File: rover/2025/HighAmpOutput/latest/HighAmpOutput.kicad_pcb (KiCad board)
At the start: 4 copper layers, 90.9 x 51 mm, 22 parts, among them J1 JST2_Pin, U1 EC5_Connector, U10 XT60PM-F, U11 XT60PM-F, U12 XT60PM-F, U2 HSS-VN7004SLHTR, U3 XT60-F, U4 XT60-F, U5 XT60-F, U6 XT60-F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

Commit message: .
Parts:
- removed U10, U11, U9: XT60PM-F, RoverFootprint:AMASS_XT60PW-F_1x02_P7.20mm_Horizontal
- added D2: R, LED_SMD:LED_0805_2012Metric_Pad1.15x1.40mm_HandSolder, F.Cu at (147.7, 83.0)
- added R2: 15k, Resistor_SMD:R_0805_2012Metric_Pad1.20x1.40mm_HandSolder, F.Cu at (147.7, 86.0)
- added R5: 1K, Resistor_SMD:R_0805_2012Metric_Pad1.20x1.40mm_HandSolder, F.Cu at (147.7, 88.9)
- added U13: XT60-F, RoverFootprint:AMASS_XT60-F_1x02_P7.20mm_Vertical, F.Cu at (164.7, 90.1)
- added U14: XT60-F, RoverFootprint:AMASS_XT60-F_1x02_P7.20mm_Vertical, F.Cu at (164.7, 100.4)
- D1: value LED -> R
- moved U4 126.8 mm to (164.7, 38.9), turned to 0 degrees
- moved U3 121.3 mm to (164.7, 28.6), turned to 0 degrees
- moved U6 108.9 mm to (164.7, 59.4), turned to 0 degrees
- moved U12 106.8 mm to (207.0, 39.9)
- moved U5 105.8 mm to (164.7, 49.1), turned to 0 degrees
- moved U1 99.3 mm to (31.8, 139.2), turned to 0 degrees
- moved J1 98.0 mm to (63.5, 153.0), turned to 0 degrees
- moved U7 94.3 mm to (164.7, 69.6), turned to 0 degrees
- moved U8 93.9 mm to (164.7, 79.9), turned to 0 degrees
- moved U2 72.1 mm to (63.3, 145.5)
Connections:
- net /Board/+24v renamed +24V
- net /Board/Vinput renamed +24V_I
- R1 pad 1: GND -> Net-(U2-FR_DIAG)
- R1 pad 2: Net-(U2-FR_DIAG) -> GND
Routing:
- net Net-(U2-INPUT): track 0.00 -> 10.9 mm
- net GND: vias 0 -> 54
- net +24V: vias 8 -> 0
- added copper zone on In1.Cu, net +24V_I
- added copper zone on B.Cu, net GND
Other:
- board size 90.9 x 51 mm -> 90.9 x 113.4 mm

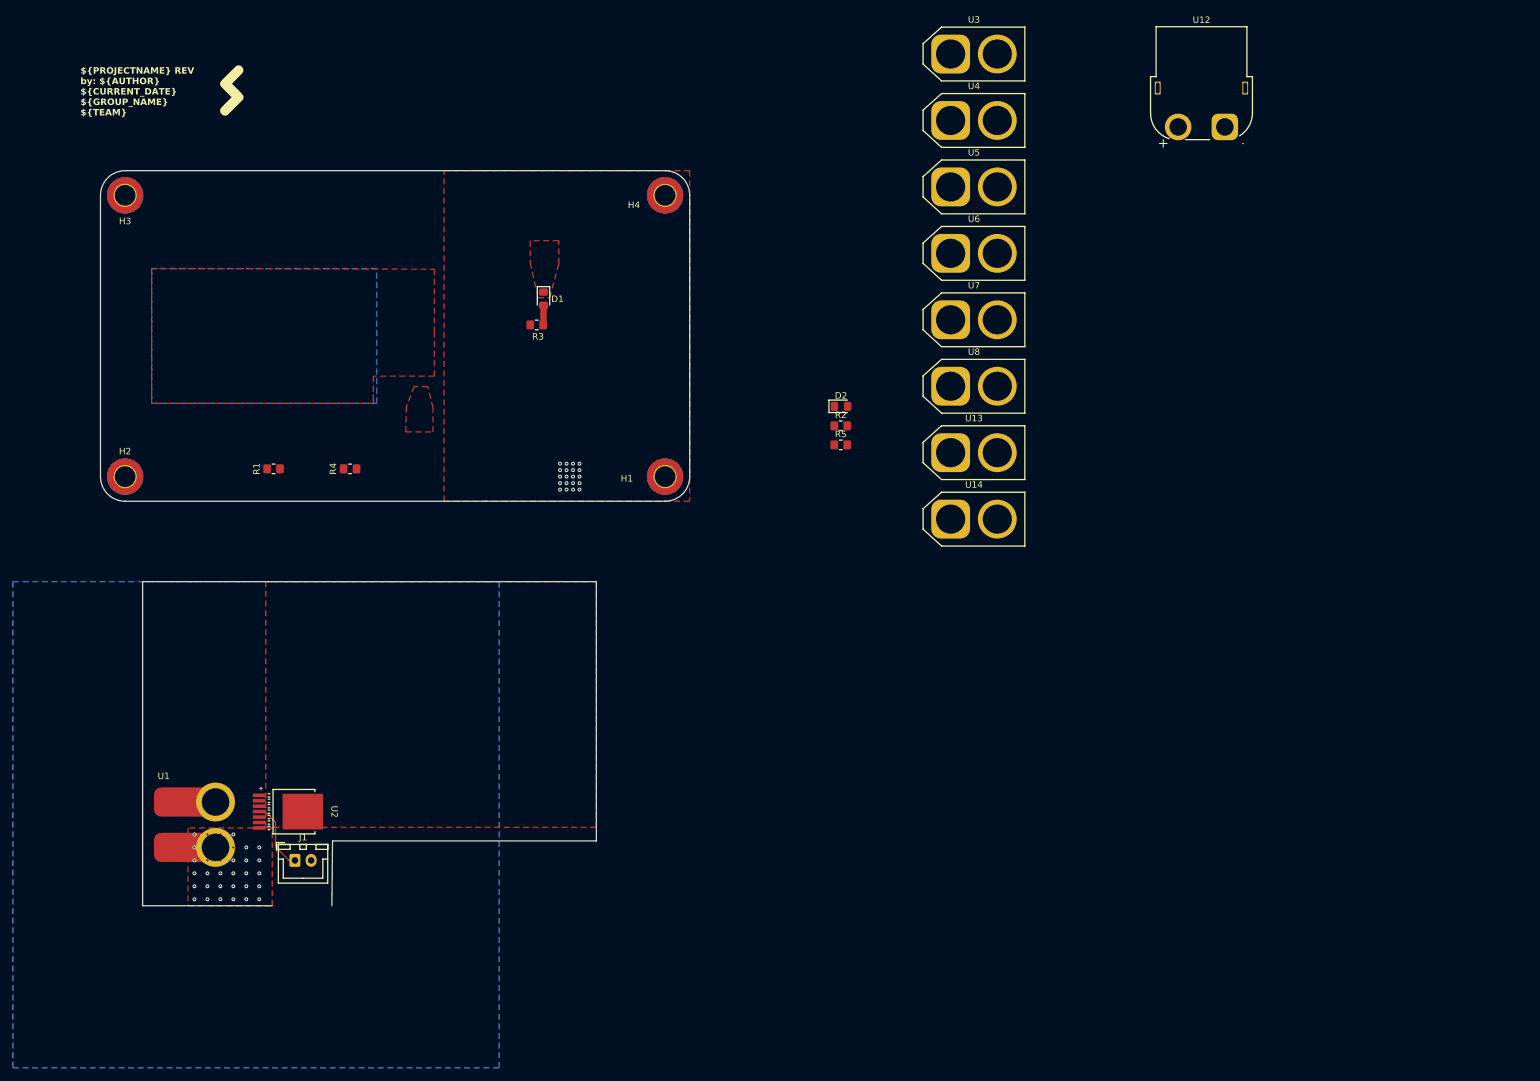
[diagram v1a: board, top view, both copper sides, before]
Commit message: Avancement PCB HighAmpOutput
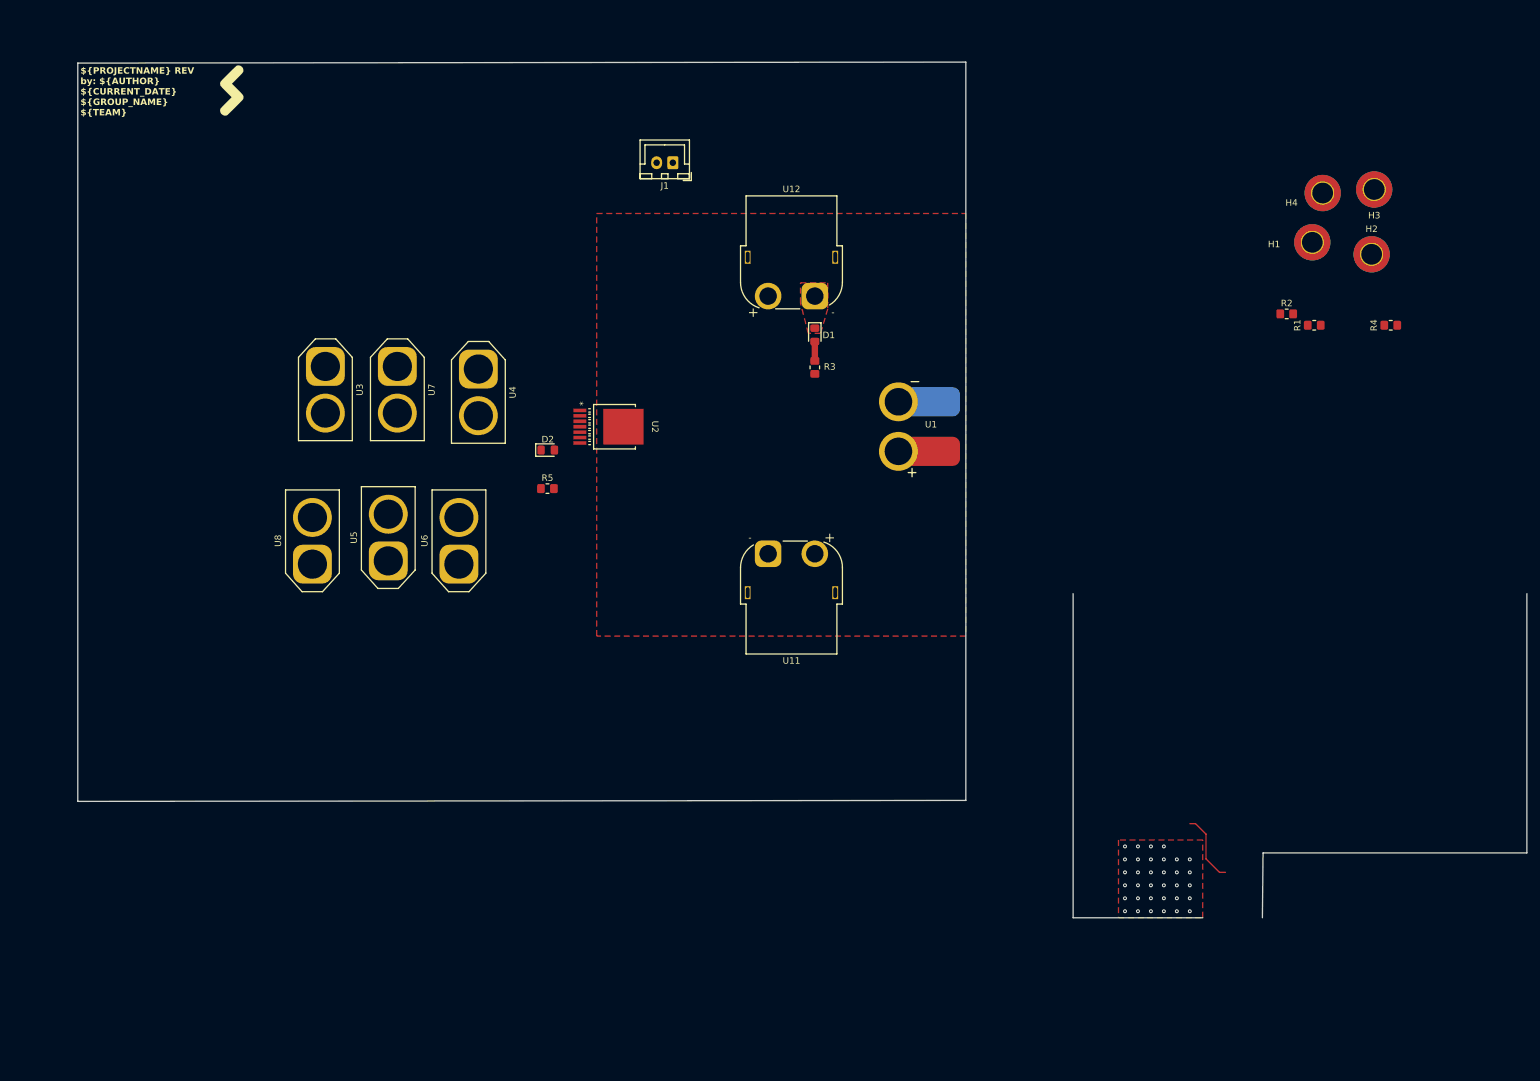
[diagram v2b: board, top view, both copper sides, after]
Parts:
- removed U13, U14: XT60-F, RoverFootprint:AMASS_XT60-F_1x02_P7.20mm_Vertical
- added U11: XT60PM-F, RoverFootprint:AMASS_XT60PW-F_1x02_P7.20mm_Horizontal, F.Cu at (136.5, 105.7)
- moved H2 195.3 mm to (229.6, 59.5)
- moved H3 192.7 mm to (230.0, 49.5)
- moved R1 162.1 mm to (220.8, 70.5)
- moved R4 162.1 mm to (232.6, 70.5)
- moved U1 141.8 mm to (166.1, 93.9), turned to 180 degrees
- moved J1 122.4 mm to (121.8, 45.4), turned to 180 degrees
- moved U3 107.8 mm to (68.2, 76.8), turned to -90 degrees
- moved H1 106.2 mm to (220.4, 57.6)
- moved U5 104.2 mm to (77.9, 106.8), turned to 90 degrees
- moved U8 102.2 mm to (66.2, 107.3), turned to 90 degrees
- moved H4 101.5 mm to (222.1, 50.0)
- moved U6 89.7 mm to (88.8, 107.3), turned to 90 degrees
- moved U7 85.7 mm to (79.3, 76.8), turned to -90 degrees
- moved U4 82.3 mm to (91.8, 77.2), turned to -90 degrees
- moved U2 77.3 mm to (112.8, 86.1)
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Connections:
- U12 pad : (no net) -> +24V_I
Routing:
- net GND: vias 54 -> 34
- removed copper zone on B.Cu, net +24V
- removed copper zone on F.Cu, net +24V
- removed copper zone on In1.Cu, net +24V_I
- removed copper zone on B.Cu, net GND
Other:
- board size 90.9 x 113.4 mm -> 223.6 x 132 mm

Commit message: PCB HighAmpOutput version final
Devrais être la version final.
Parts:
- added G***: LOGO, LOGO, F.Cu at (113.5, 77.5)
- moved H4 176.7 mm to (59.7, 119.8)
- moved H3 170.5 mm to (59.7, 58.1)
- moved R4 141.0 mm to (99.3, 116.5), turned to -90 degrees
- moved R1 132.4 mm to (96.8, 117.3), turned to -90 degrees
- moved R2 116.5 mm to (100.0, 67.4), turned to 180 degrees
- moved H2 109.6 mm to (138.1, 119.8)
- moved H1 82.4 mm to (138.1, 58.1)
- moved U2 29.0 mm to (107.6, 114.7)
- moved J1 27.1 mm to (101.5, 63.2)
- moved U1 24.6 mm to (141.7, 97.0)
- moved U12 24.6 mm to (119.3, 69.0)
- moved D1 17.4 mm to (126.5, 69.0), turned to 0 degrees
- moved U11 16.2 mm to (120.7, 108.8)
- moved R3 14.5 mm to (131.6, 69.0), turned to 180 degrees
- moved D2 11.9 mm to (96.8, 100.2)
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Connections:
- H1 pad 1: unconnected-(H1-Pad1)_2 -> GND
- H2 pad 1: unconnected-(H2-Pad1)_2 -> GND
- H3 pad 1: unconnected-(H3-Pad1)_1 -> GND
- H4 pad 1: unconnected-(H4-Pad1)_1 -> GND
- U11 pad : +24V_I -> (no net)
- U12 pad : +24V_I -> (no net)
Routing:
- net Net-(U2-INPUT): track 10.9 -> 55.4 mm
- net Net-(U2-FR_DIAG): track 0.00 -> 5.64 mm
- net GND: track 0.00 -> 4.05 mm, vias 34 -> 3
- net Net-(U2-CS): track 0.00 -> 2.95 mm
- net Net-(D2-A): track 0.00 -> 2.53 mm
- added copper zone on F.Cu, net +24V
- added copper zone on B.Cu, net GND
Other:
- board size 223.6 x 132 mm -> 87.8 x 70.7 mm
- copper layers 4 -> 2

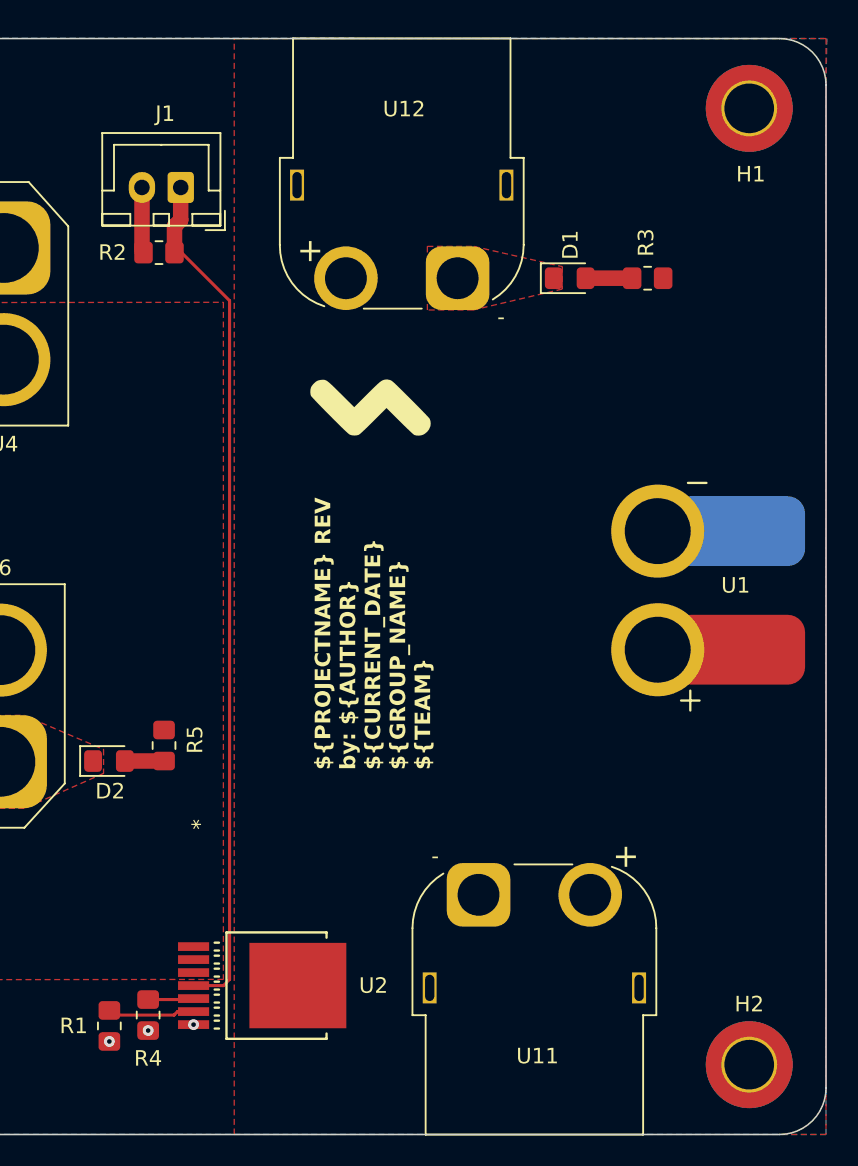
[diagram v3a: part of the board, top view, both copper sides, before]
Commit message: Correction PCB HighAmpOutput
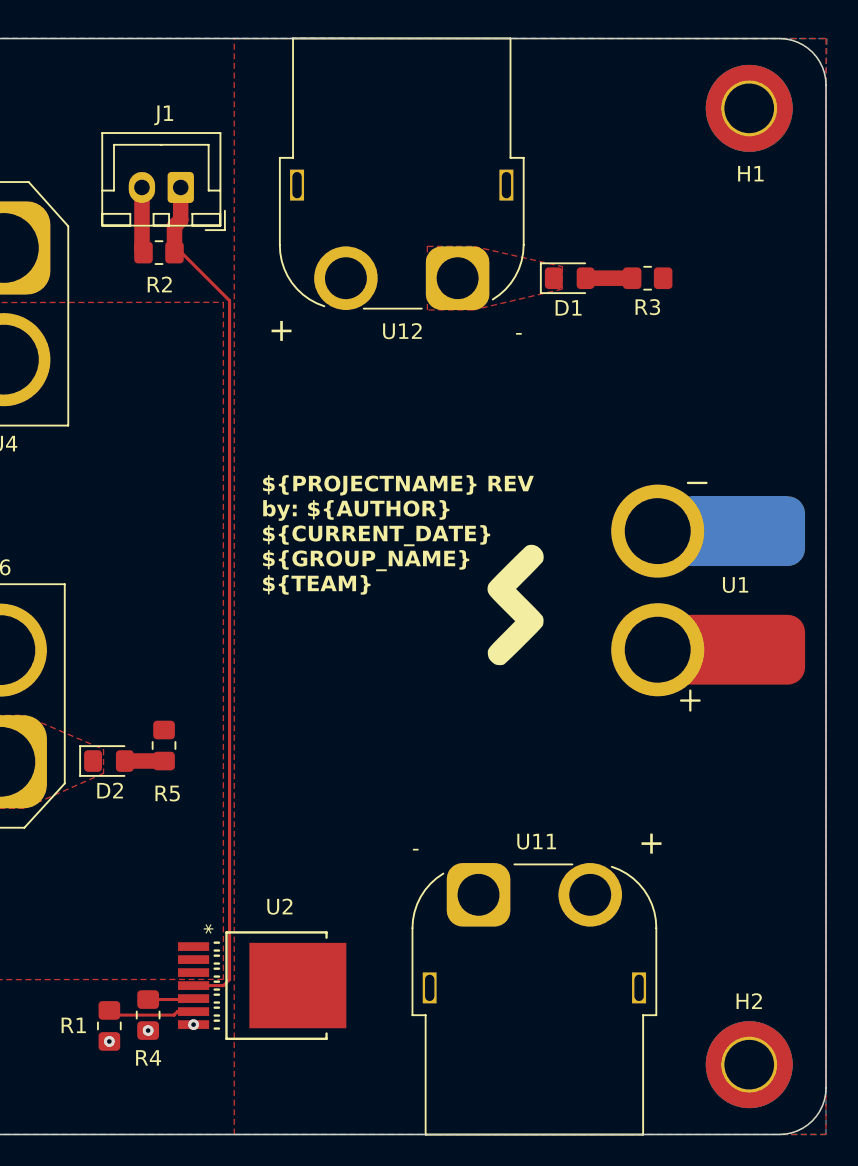
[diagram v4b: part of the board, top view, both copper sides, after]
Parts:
- moved G*** 16.1 mm to (123.2, 90.3), turned to 180 degrees
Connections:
- U11 pad : (no net) -> +24V_I
- U12 pad : (no net) -> +24V_I
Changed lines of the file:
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@@
 		(tags "resistor handsolder")
 		(property "Reference" "R3"
-			(at 0.1 2.3 90)
+			(at 0 -1.9 180)
 			(layer "F.SilkS")
 			(effects
@@
 		)
 		(property "Value" "1K"
-			(at 0 1.65 360)
+			(at 0 1.65 0)
 			(layer "F.Fab")
 			(effects
@@
 		)
 		(fp_text user "${REFERENCE}"
-			(at 0 0 360)
+			(at 0 0 0)
 			(layer "F.Fab")
 			(effects
@@
 		(tags "VN7004SLHTR ")
 		(property "Reference" "U2"
-			(at 0 -6.25 0)
+			(at -5.05295 -0.2245 0)
 			(unlocked yes)
 			(layer "F.SilkS")
@@
 		)
 		(fp_text user "*"
-			(at -10.3937 5.4217 -90)
+			(at -3.65295 4.6255 -90)
 			(unlocked yes)
 			(layer "F.SilkS")
@@
 	(footprint "LOGO"
 		(layer "F.Cu")
-		(at 113.45 77.55 90)
+		(at 123.2 90.35 180)
 		(property "Reference" "G***"
-			(at 4.760877 0 90)
+			(at 4.760877 0 360)
 			(layer "F.SilkS")
 			(hide yes)
@@
 		)
 		(property "Value" "LOGO"
-			(at 0.075 0 90)
+			(at 0.075 0 360)
 			(layer "F.SilkS")
 			(hide yes)
@@
 		)
 		(property "Footprint" ""
-			(at 0 0 90)
+			(at 0 0 360)
 			(layer "F.Fab")
 			(hide yes)
@@
 		)
 		(property "Datasheet" ""
-			(at 0 0 90)
+			(at 0 0 360)
 			(layer "F.Fab")
 			(hide yes)
@@
 		)
 		(property "Description" ""
-			(at 0 0 90)
+			(at 0 0 360)
 			(layer "F.Fab")
 			(hide yes)
@@
 		(tags "RC Connector XT60")
 		(property "Reference" "U12"
-			(at -3.45 -10.9 0)
+			(at -3.55 3.45 0)
 			(layer "F.SilkS")
 			(effects
@@
 		)
 		(fp_text user "+"
-			(at -9.5 -1.79705 0)
+			(at -11.35 3.35 0)
 			(layer "F.SilkS")
 			(effects
@@
 		)
 		(fp_text user "-"
-			(at 2.8 2.5 0)
+			(at 3.95 3.5 0)
 			(layer "F.SilkS")
 			(effects
@@
 			(layers "*.Cu" "*.Mask")
 			(remove_unused_layers no)
+			(net 7 "+24V_I")
 		)
 		(pad "" thru_hole rect
@@
 			(layers "*.Cu" "*.Mask")
 			(remove_unused_layers no)
+			(net 7 "+24V_I")
 		)
 		(pad "1" thru_hole roundrect
@@
 		(tags "resistor handsolder")
 		(property "Reference" "R5"
-			(at -0.375 -2 90)
+			(at 3.125 -0.225 180)
 			(layer "F.SilkS")
 			(effects
@@
 		(tags "mounting hole 3.2mm m3 din965")
 		(property "Reference" "H2"
-			(at 0 -3.9 0)
+			(at 0 -4.05 0)
 			(layer "F.SilkS")
 			(effects
@@
 		(tags "RC Connector XT60")
 		(property "Reference" "U11"
-			(at -3.8 -10.4 0)
+			(at -3.75 3.4 0)
 			(layer "F.SilkS")
 			(effects
@@
 		)
 		(fp_text user "-"
-			(at 2.8 2.5 0)
+			(at 4.05 3 0)
 			(layer "F.SilkS")
 			(effects
@@
 		)
 		(fp_text user "+"
-			(at -9.5 2.5 0)
+			(at -11.15 3.35 0)
 			(layer "F.SilkS")
 			(effects
@@
 			(layers "*.Cu" "*.Mask")
 			(remove_unused_layers no)
+			(net 7 "+24V_I")
 		)
 		(pad "" thru_hole rect
@@
 			(layers "*.Cu" "*.Mask")
 			(remove_unused_layers no)
+			(net 7 "+24V_I")
 		)
 		(pad "1" thru_hole roundrect
@@
 		(tags "LED handsolder")
 		(property "Reference" "D1"
-			(at 0.05 -2.15 90)
+			(at -0.075 1.95 180)
 			(layer "F.SilkS")
 			(effects
@@
 		)
 		(property "Value" "R"
-			(at 0 1.65 360)
+			(at 0 1.65 0)
 			(layer "F.Fab")
 			(effects
@@
 		)
 		(fp_text user "${REFERENCE}"
-			(at 0 0 360)
+			(at 0 0 0)
 			(layer "F.Fab")
 			(effects
@@
 		(tags "LED handsolder")
 		(property "Reference" "D2"
-			(at 0.075 1.95 360)
+			(at 0.075 1.95 0)
 			(layer "F.SilkS")
 			(effects
@@
 		)
 		(property "Value" "R"
-			(at 0 1.65 360)
+			(at 0 1.65 0)
 			(layer "F.Fab")
 			(effects
@@
 		)
 		(fp_text user "${REFERENCE}"
-			(at 0 0 360)
+			(at 0 0 0)
 			(layer "F.Fab")
 			(effects
@@
 		(tags "resistor handsolder")
 		(property "Reference" "R2"
-			(at 3 0 360)
+			(at -0.05 -2.1 0)
 			(layer "F.SilkS")
 			(effects
@@
 		)
 		(property "Value" "15k"
-			(at 0 1.65 360)
+			(at 0 1.65 0)
 			(layer "F.Fab")
 			(effects
@@
 		)
 		(fp_text user "${REFERENCE}"
-			(at 0 0 360)
+			(at 0 0 0)
 			(layer "F.Fab")
 			(effects
@@
 	)
 	(gr_text "${PROJECTNAME} REV${REVISION}\nby: ${AUTHOR}\n${CURRENT_DATE}\n${GROUP_NAME}\n${TEAM}"
-		(at 117.65 100.75 90)
+		(at 106.65 89.35 0)
 		(layer "F.SilkS")
 		(effects
@@
 		)
 		(height -5.1)
-		(gr_text "10,3000 mm"
+		(gr_text "10.3000 mm"
 			(at 126.1 76.9 90)
 			(layer "User.1")
@@
 		)
 		(height -1.7)
-		(gr_text "32,9500 mm"
+		(gr_text "32.9500 mm"
 			(at 96.15 87.075 90)
 			(layer "User.1")
@@
 		)
 		(height -10.45)
-		(gr_text "1,2000 mm"
+		(gr_text "1.2000 mm"
 			(at 150.95 54.05 90)
 			(layer "User.1")
@@
 		)
 		(height -9.85)
-		(gr_text "5,1000 mm"
+		(gr_text "5.1000 mm"
 			(at 150.55 64.15 90)
 			(layer "User.1")
@@
 		)
 		(height -13.7)
-		(gr_text "17,4000 mm"
+		(gr_text "17.4000 mm"
 			(at 125.65 97.55 90)
 			(layer "User.1")
@@
 		)
 		(height 4.9)
-		(gr_text "3,7000 mm"
+		(gr_text "3.7000 mm"
 			(at 83.75 112.4 90)
 			(layer "User.1")
@@
 		)
 		(height -9.5)
-		(gr_text "5,1000 mm"
+		(gr_text "5.1000 mm"
 			(at 149.4 114 90)
 			(layer "User.1")
@@
 		)
 		(height -11.9)
-		(gr_text "1,2000 mm"
+		(gr_text "1.2000 mm"
 			(at 151.85 123.75 90)
 			(layer "User.1")
@@
 		)
 		(height 2.9)
-		(gr_text "1,9500 mm"
+		(gr_text "1.9500 mm"
 			(at 123.85 112.325 90)
 			(layer "User.2")
@@
 		)
 		(height -15.7)
-		(gr_text "1,8000 mm"
+		(gr_text "1.8000 mm"
 			(at 116 65.6 90)
 			(layer "User.2")
@@
 		)
 		(height -9.8)
-		(gr_text "11,7000 mm"
+		(gr_text "11.7000 mm"
 			(at 98.7 83.65 90)
 			(layer "User.2")
@@
 		)
 		(height 12.909739)
-		(gr_text "7,9600 mm"
+		(gr_text "7.9600 mm"
 			(at 145.314728 120.262337 -89.92802042)
 			(layer "User.2")
@@
 		)
 		(height -18.15)
-		(gr_text "8,0000 mm"
+		(gr_text "8.0000 mm"
 			(at 146.95 57.6 90)
 			(layer "User.2")
@@
 		)
 		(height -16.7)
-		(gr_text "9,7000 mm"
+		(gr_text "9.7000 mm"
 			(at 105.35 101.35 90)
 			(layer "User.2")
@@
 		)
 		(height 1.899999)
-		(gr_text "4,5000 mm"
+		(gr_text "4.5000 mm"
 			(at 164.75 50.150001 0)
 			(layer "User.3")
@@
 		)
 		(height 15.5)
-		(gr_text "3,0000 mm"
+		(gr_text "3.0000 mm"
 			(at 146.55 94.5 90)
 			(layer "User.3")
@@
 		)
 		(height -4.6)
-		(gr_text "4,5000 mm"
+		(gr_text "4.5000 mm"
 			(at 170.45 52.75 90)
 			(layer "User.3")
@@
 		)
 		(height -8.7)
-		(gr_text "4,5000 mm"
+		(gr_text "4.5000 mm"
 			(at 170.15 55.5 90)
 			(layer "User.3")
@@
 		)
 		(height 3.85)
-		(gr_text "4,5000 mm"
+		(gr_text "4.5000 mm"
 			(at 164.75 45.5 0)
 			(layer "User.3")
@@
 		)
 		(height -3.1)
-		(gr_text "10,1500 mm"
+		(gr_text "10.1500 mm"
 			(at 139.35 58.275 90)
 			(layer "User.3")
@@
 		)
 		(height 3.4)
-		(gr_text "4,5000 mm"
+		(gr_text "4.5000 mm"
 			(at 169.25 118.9 90)
 			(layer "User.3")
